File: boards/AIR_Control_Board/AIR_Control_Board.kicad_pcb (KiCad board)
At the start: 2 copper layers, 77 parts, among them IC1 ATMEGA16M1, J1 AIR-, J2 Ultrafit_2, J3 To Interface Board, J4 PrechargeRelay, J5 AIR+, J6 CONN_02X03, Q1 NMOS_GSD_30V, Q2 NMOS_GSD_30V, Q3 NMOS_GSD_30V, Q4 NMOS_GSD_30V, Q5 NMOS_GSD_30V, Q6 NMOS_GSD_30V, Q7 NMOS_GSD_30V, U1 CAN_Transceiver, U2 TPS561201, Y1 Crystal_SMD

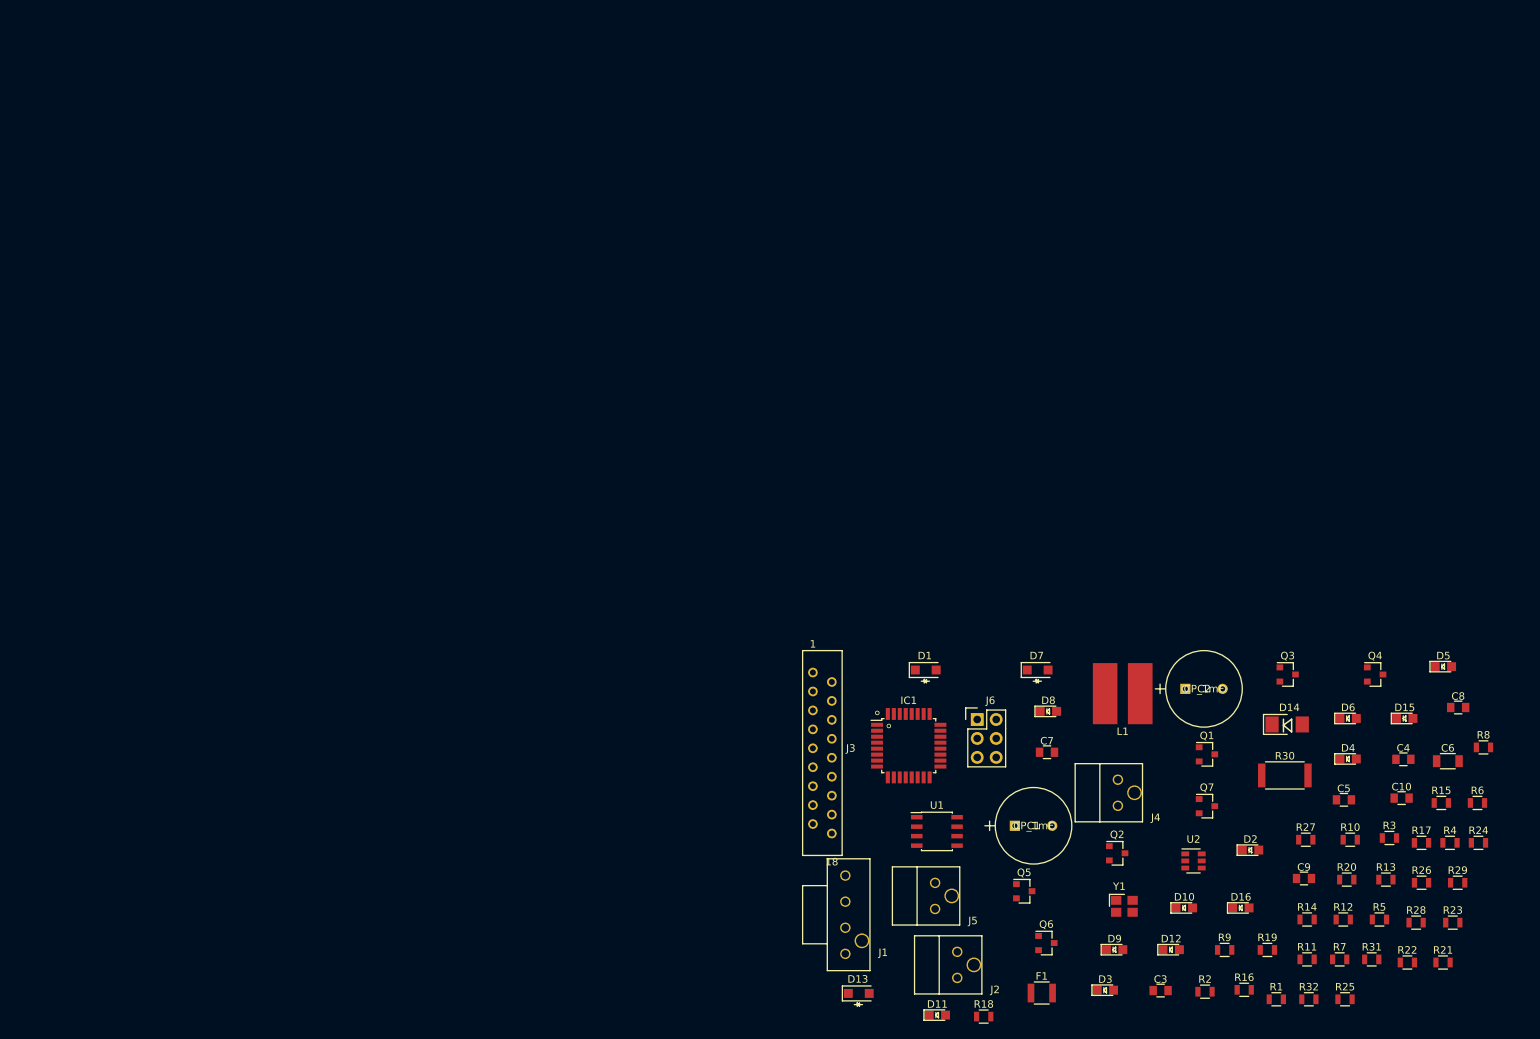
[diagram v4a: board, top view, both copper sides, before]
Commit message: replaced all files besides BMS with most updated files from upstream
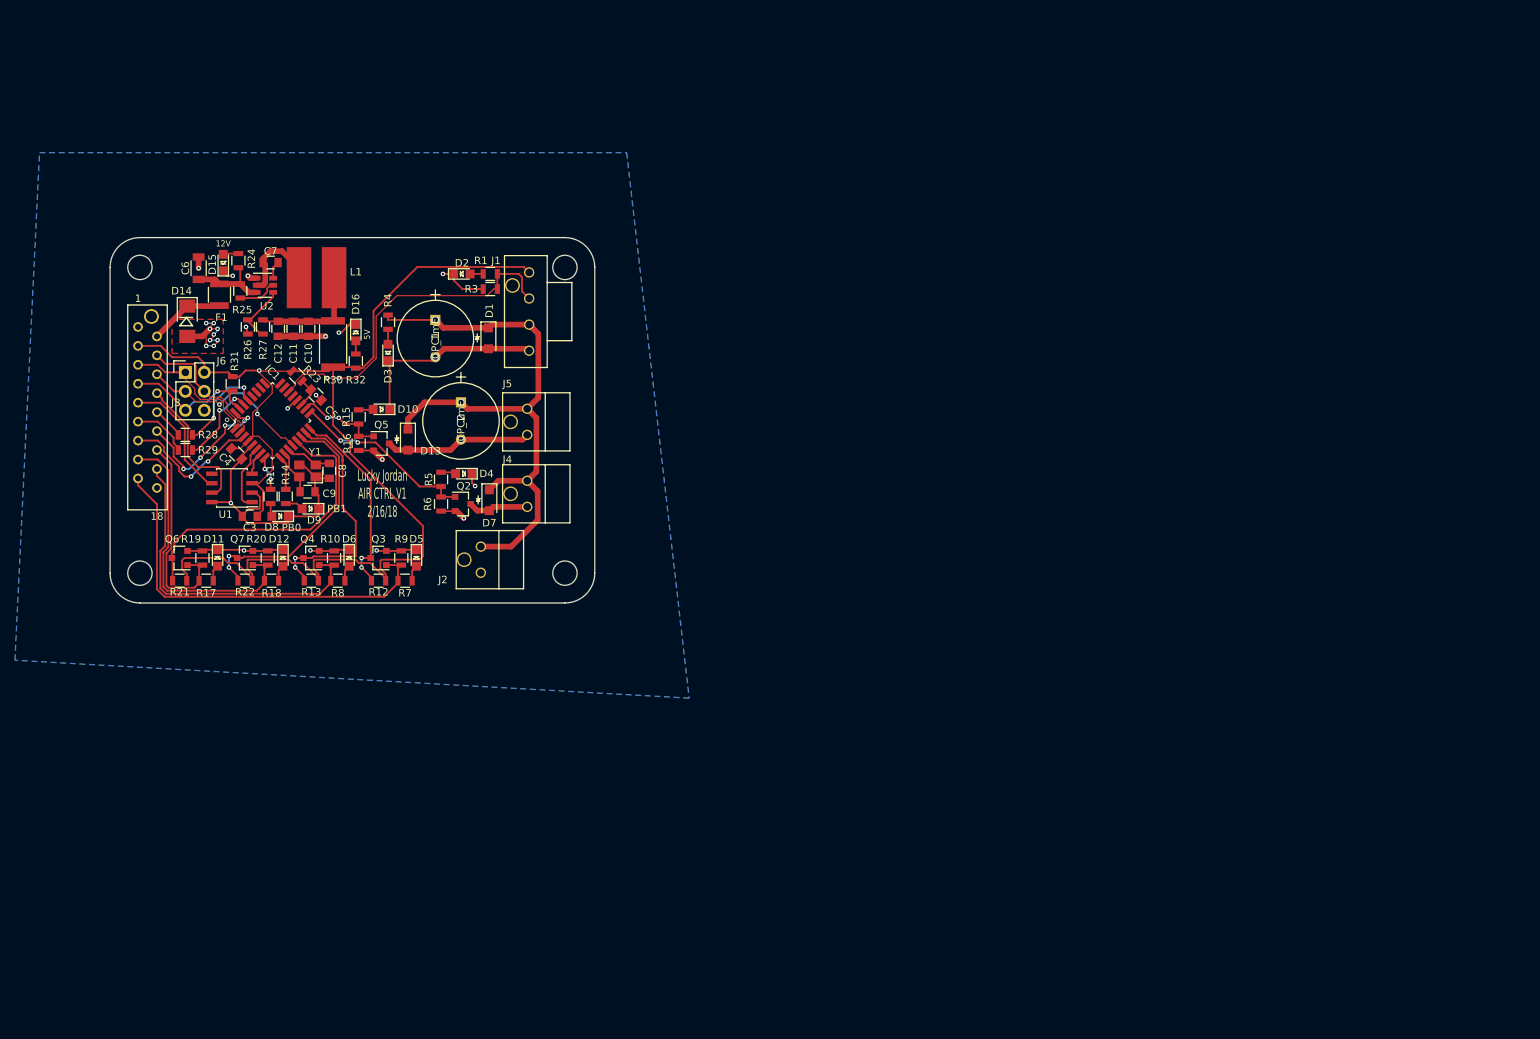
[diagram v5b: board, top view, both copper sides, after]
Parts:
- removed Q1: NMOS_GSD_30V, footprints:SOT-23F
- removed R2: R_100k, footprints:R_0805_OEM
- added C11: C_1uF, footprints:C_0805_OEM, F.Cu at (88.1, 66.3)
- added C12: C_0.1uF, footprints:C_0805_OEM, F.Cu at (86.1, 66.3)
- J3: value To Interface Board -> micromatch_female_TOP_ENTRY_locking_18; footprint footprints:micromatch_female_ra_18 -> footprints:micromatch_female_vert_18
- R1: value R_1k -> R_200
- moved R24 183.7 mm to (80.8, 57.1), turned to 90 degrees
- moved R29 180.2 mm to (73.7, 82.5)
- moved C6 180.1 mm to (75.4, 58.2), turned to 90 degrees
- moved R28 177.5 mm to (73.7, 80.5), turned to 180 degrees
- moved R21 177.0 mm to (72.9, 100.1), turned to 180 degrees
- moved R25 176.0 mm to (81.0, 61.2), turned to 270 degrees
- moved R26 174.2 mm to (82.0, 66.0), turned to 270 degrees
- moved R23 171.4 mm to (88.6, 72.6), turned to 315 degrees
- moved R31 171.1 mm to (80.0, 73.7), turned to 270 degrees
- moved D15 169.8 mm to (78.7, 57.4), turned to 90 degrees
- moved R17 166.7 mm to (76.5, 100.1), turned to 180 degrees
- moved R22 164.1 mm to (81.7, 100.1), turned to 180 degrees
- moved C4 161.8 mm to (80.5, 83.1), turned to 315 degrees
- moved C10 159.5 mm to (90.2, 66.3), turned to 270 degrees
- moved R4 158.6 mm to (100.8, 65.4), turned to 270 degrees
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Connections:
- IC1 pad 17: /AIR+LSD -> /PrechargeCTL
- IC1 pad 18: /PrechargeCTL -> /AIR+LSD
- IC1 pad 29: /IMDStatus -> Net-(IC1-Pad29)
- IC1 pad 3: Net-(IC1-Pad3) -> /BMSStatus
- IC1 pad 30: /BMSStatus -> Net-(IC1-Pad30)
- IC1 pad 32: Net-(IC1-Pad32) -> /IMDStatus
- J1 pad 1: /12V_Fused -> VCC
- J1 pad 2: /Aux_Contact- -> /AIR-_Weld_Detect
- J3 pad 12: /ShutdownSenseBMS -> /IMDStatus
- J3 pad 13: /ShutdownSenseIMD -> /BMSStatus
- J3 pad 14: /ShutdownSenseMainTSConn -> /ShutdownSenseBMS
- J3 pad 15: /ShutdownSenseConnToHVD -> /ShutdownSenseIMD
- J3 pad 16: /IMDStatus -> /ShutdownSenseMainTSConn
- J3 pad 17: /BMSStatus -> /ShutdownSenseConnToHVD
- J4 pad 1: Net-(D7-Pad2) -> /ShutdownIn
- J4 pad 2: /ShutdownIn -> Net-(D7-Pad2)
- R1 pad 1: Net-(D2-Pad2) -> /AIR-_Weld_Detect
- R1 pad 2: /Aux_Contact- -> Net-(D2-Pad2)
- R28 pad 1: Net-(IC1-Pad27) -> Net-(IC1-Pad29)
- R29 pad 2: Net-(IC1-Pad28) -> Net-(IC1-Pad30)
- R3 pad 1: VCC -> /AIR-_Weld_Detect
- R3 pad 2: /AIR-_Weld_Detect -> GND
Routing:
- net VCC: track 0.00 -> 176.5 mm, vias 0 -> 1
- net GND: track 0.00 -> 139.7 mm, vias 0 -> 25
- net /ShutdownIn: track 0.00 -> 82.4 mm
- net /ShutdownSenseConnToHVD: track 0.00 -> 54.0 mm
- net /AIR-_Weld_Detect: track 0.00 -> 46.5 mm, vias 0 -> 2
- net /ShutdownSenseMainTSConn: track 0.00 -> 45.1 mm
- net /SenseBMS: track 0.00 -> 41.5 mm
- net /ShutdownSenseIMD: track 0.00 -> 39.4 mm
- net /SenseIMD: track 0.00 -> 34.7 mm, vias 0 -> 2
- net /SenseMainTSConn: track 0.00 -> 32.8 mm, vias 0 -> 2
- net /ShutdownSenseBMS: track 0.00 -> 28.6 mm
- net /SenseConnToHVD: track 0.00 -> 26.7 mm, vias 0 -> 2
- net /PrechargeCTL: track 0.00 -> 25.0 mm, vias 0 -> 2
- net /SCK: track 0.00 -> 23.9 mm, vias 0 -> 2
- net /IMDStatus: track 0.00 -> 20.6 mm, vias 0 -> 4
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- added copper zone on B.Cu, net GND
- added copper zone on F.Cu, net GND
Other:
- board outline added: 65 x 49 mm
- net class Default: trace_width 0.254 -> 0.1524
- rule trace_min: 0.254 -> 0.1524
- board text added: "12V"
- board text added: "5V"
- board text added: "Lucky Jordan AIR CTRL V1 2/16/18"
- board text added: "OLIN ELECTRIC MOTORSPORTS MK. III"
- board text added: "PB0"
- board text added: "PB1"
